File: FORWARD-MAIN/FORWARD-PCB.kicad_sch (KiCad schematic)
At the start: 50 parts, among them J1 USB_B_Micro, J3 Conn_01x13_Socket, J4 Conn_01x08_Socket, J5 Screw_Terminal_01x03, Q1 SS8050-G, Q2 SS8050-G, U2 CP2102N-Axx-xQFN28, U5 ESP32-WROOM-32D

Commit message: PCB order rev 1.0
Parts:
- removed J3: Conn_01x13_Socket, Connector_Phoenix_MSTB:PhoenixContact_MSTBA_2,5_13-G_1x13_P5.00mm_Horizontal, symbol Connector:Conn_01x13_Socket
- removed R15, R19: 3.2k, Resistor_SMD:R_0805_2012Metric, symbol Device:R_US
- removed TP4: TestPoint, Connector_PinHeader_2.54mm:PinHeader_1x01_P2.54mm_Vertical, symbol Connector:TestPoint
- added J2: Conn_01x14_Socket, Connector_PinSocket_2.54mm:PinSocket_1x14_P2.54mm_Horizontal, symbol Connector:Conn_01x14_Socket
- added J3, J6: Conn_01x02_Pin, Connector_PinSocket_2.54mm:PinSocket_1x02_P2.54mm_Vertical, symbol Connector:Conn_01x02_Pin
- Boot1, Reset1: footprint Button_Switch_SMD:SW_Tactile_SPST_NO_Straight_CK_PTS636Sx25SMTRLFS -> Button_Switch_SMD:SW_SPST_TL3305A
- D6: value LED -> Power-LED
- J5: footprint TerminalBlock_MetzConnect:TerminalBlock_MetzConnect_Type086_RT03403HBLC_1x03_P3.81mm_Horizontal -> TerminalBlock_Phoenix:TerminalBlock_Phoenix_MPT-0,5-3-2.54_1x03_P2.54mm_Horizontal
- R12: value 22.1k -> 1k
- R13: value 47.5k -> 1k
- R14: value 2k -> 10k
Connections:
- net +3.3V: now also J6.1 (Pin_1), J6.2 (Pin_2)
- net +5V: now also U2.8 (VBUS); no longer C3.1, C5.1, R14.2, U2.6 (VDD)
- net GND: now also R12.1, R13.2, J2.14 (Pin_14); no longer D6.1 (K), R13.1
- net Haptics-ENA_PWM: now also J2.5 (Pin_5)
- net Haptics-ENB_PWM: now also J2.6 (Pin_6)
- net Haptics-IN1: now also J2.1 (Pin_1)
- net Haptics-IN2: now also J2.2 (Pin_2)
- net Haptics-IN3: now also J2.3 (Pin_3)
- net Haptics-IN4: now also J2.4 (Pin_4)
- net IO0: now also U5.25 (IO0); no longer D4.2 (A)
- net LIGHT-IO4-26: now also D4.2 (A), U5.24 (IO2), J2.9 (Pin_9); no longer U5.26 (IO4)
- net P0W-IO13-16: now also J2.7 (Pin_7)
- net PHOTO-IO2-24: now also U5.26 (IO4), J2.8 (Pin_8); no longer U5.24 (IO2)
- net SCL: now also J3.2 (Pin_2)
- net SDA: now also J3.1 (Pin_1)
- net VBUS: no longer R12.1
- net Wheel_L_LPWM: now also J2.10 (Pin_10)
- net Wheel_L_RPWM: now also J2.11 (Pin_11)
- net Wheel_R_LPWM: now also J2.12 (Pin_12)
- net Wheel_R_RPWM: now also J2.13 (Pin_13)
- net at D4.1 (K): now also R12.2; no longer U5.25 (IO0)
- new net: C3.1, C5.1, R14.2, U2.6 (VDD)
- new net: D6.1 (K), R13.1
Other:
- moved on the sheet: C10, C3, C4, C5, D6, J5, R16, R17, R18, R20

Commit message: MAIN PCB rev 2.0
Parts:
- J1: footprint Connector_USB:USB_Micro-B_Molex-105133-0031 -> Connector_USB:USB_Micro-B_Wuerth_629105150521

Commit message: backups
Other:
- note added: "Harmonic Cancellation"
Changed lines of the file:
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@@
 	)
 	(rectangle
-		(start 16.51 143.51)
-		(end 58.42 190.5)
+		(start 22.86 152.4)
+		(end 49.53 181.61)
 		(stroke
 			(width 0)
@@
 		)
 	)
+	(text "Harmonic Cancellation"
+		(exclude_from_sim no)
+		(at 68.834 158.75 0)
+		(effects
+			(font
+				(size 1.27 1.27)
+			)
+			(justify left bottom)
+		)
+	)
 	(text "output only"
 		(exclude_from_sim no)
@@
 	(text "3.3V communication"
 		(exclude_from_sim no)
-		(at 27.94 27.94 0)
+		(at 50.038 23.368 0)
 		(effects
 			(font
@@
 	(text "IMU"
 		(exclude_from_sim no)
-		(at 17.78 147.32 0)
+		(at 28.194 158.496 0)
 		(effects
 			(font
@@
 		(dnp no)
 		(property "Reference" "J2"
-			(at 161.29 170.1799 0)
+			(at 161.036 175.006 0)
 			(effects
 				(font
@@
 		)
 		(property "Value" "Conn_01x14_Socket"
-			(at 161.29 172.7199 0)
+			(at 161.29 172.7199 90)
 			(effects
 				(font

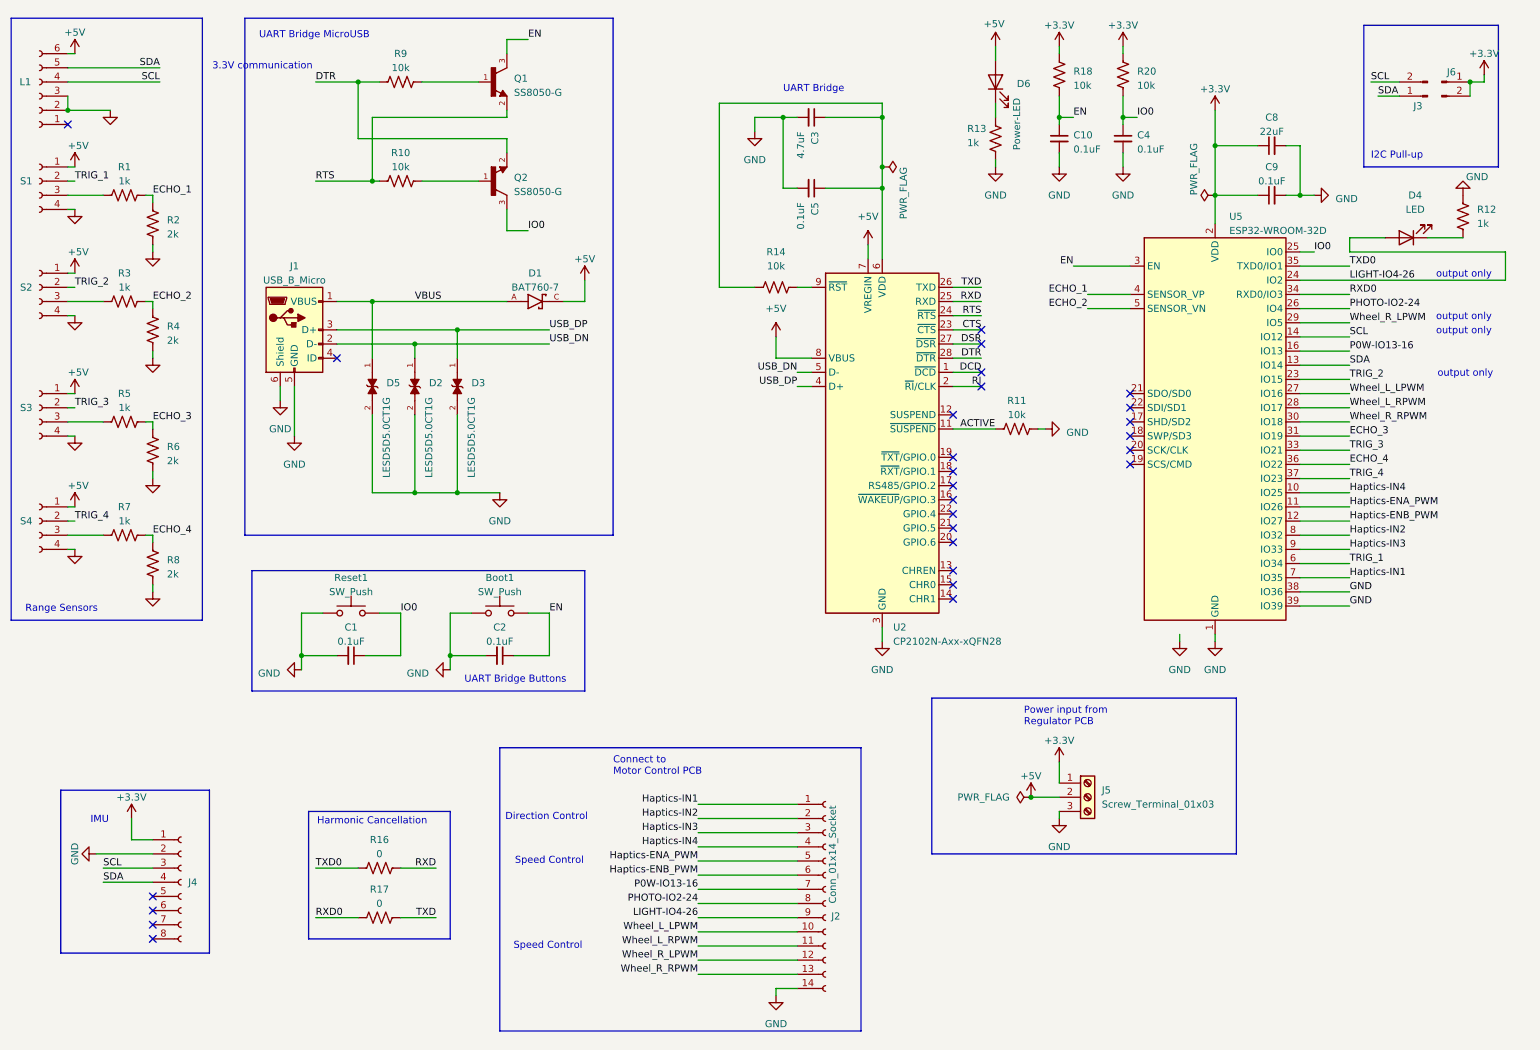
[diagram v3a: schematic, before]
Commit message: fix i2c but still an issue
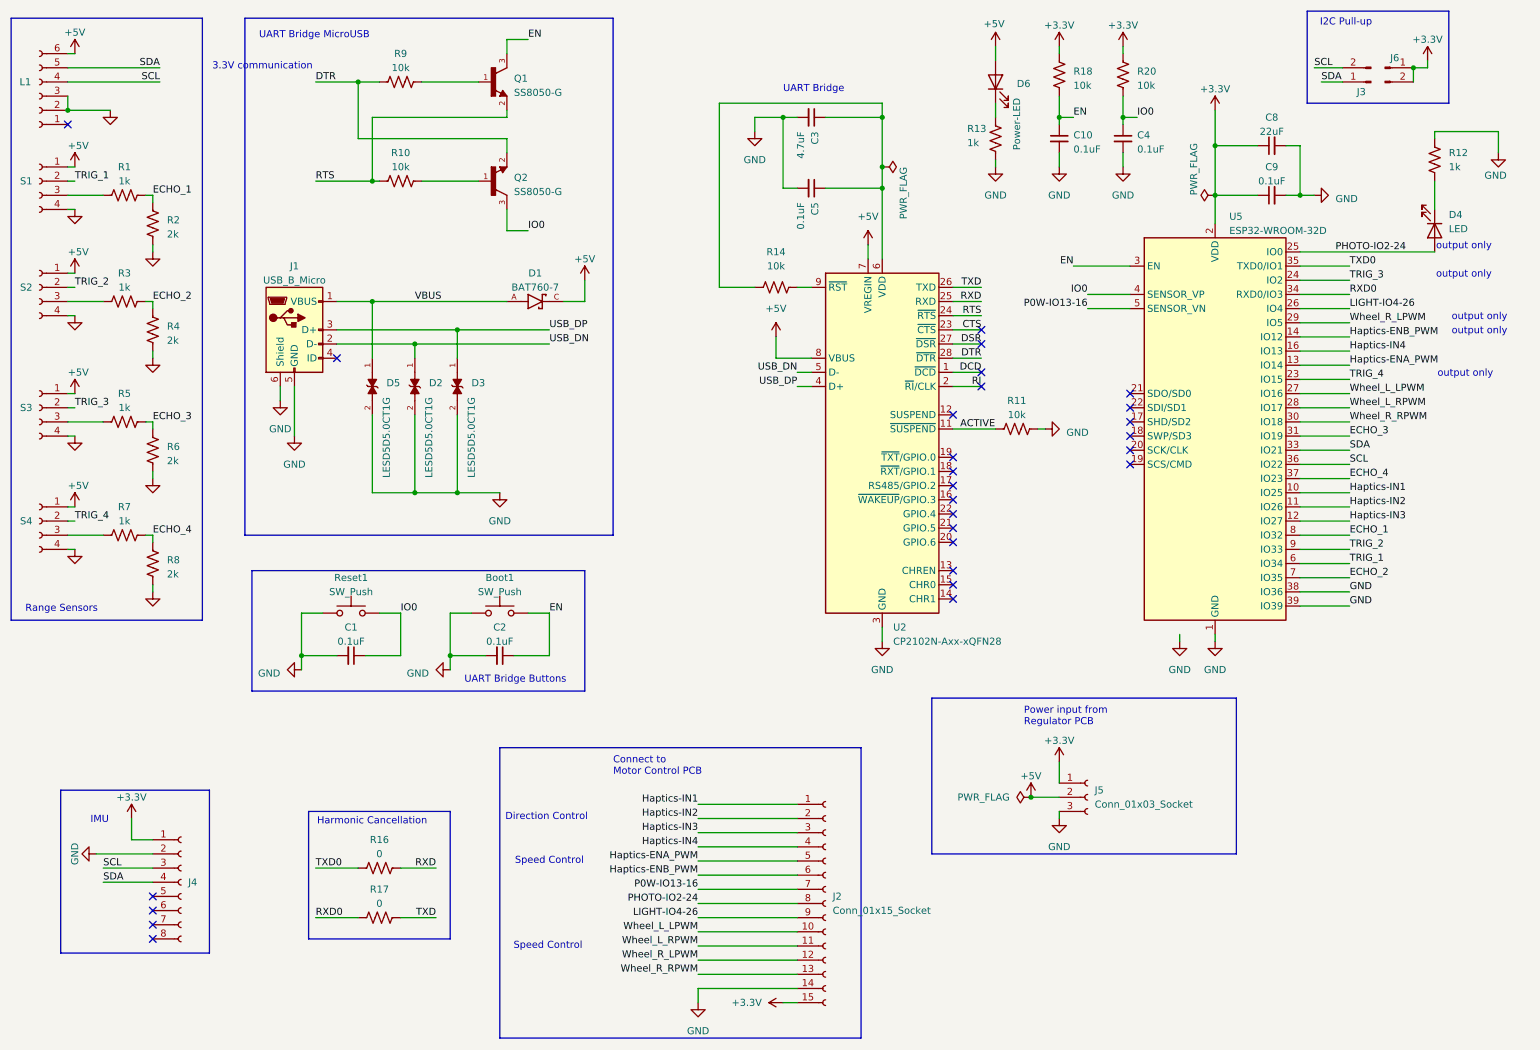
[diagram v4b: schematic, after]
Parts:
- removed J2: Conn_01x14_Socket, Connector_PinSocket_2.54mm:PinSocket_1x14_P2.54mm_Horizontal, symbol Connector:Conn_01x14_Socket
- removed J5: Screw_Terminal_01x03, TerminalBlock_Phoenix:TerminalBlock_Phoenix_MPT-0,5-3-2.54_1x03_P2.54mm_Horizontal, symbol Connector:Screw_Terminal_01x03
- added J2: Conn_01x15_Socket, Connector_PinSocket_2.54mm:PinSocket_1x15_P2.54mm_Horizontal, symbol Connector:Conn_01x15_Socket
- added J5: Conn_01x03_Socket, Connector_PinSocket_2.54mm:PinSocket_1x03_P2.54mm_Horizontal, symbol Connector:Conn_01x03_Socket
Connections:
- net +3.3V: now also J2.15 (Pin_15), J5.1 (Pin_1)
- net +5V: now also J5.2 (Pin_2)
- net ECHO_1: now also U5.8 (IO32); no longer U5.4 (SENSOR_VP)
- net ECHO_2: now also U5.7 (IO35); no longer U5.5 (SENSOR_VN)
- net ECHO_4: now also U5.37 (IO23); no longer U5.36 (IO22)
- net GND: now also J2.14 (Pin_14), J5.3 (Pin_3)
- net Haptics-ENA_PWM: now also U5.13 (IO14), J2.5 (Pin_5); no longer U5.11 (IO26)
- net Haptics-ENB_PWM: now also U5.14 (IO12), J2.6 (Pin_6); no longer U5.12 (IO27)
- net Haptics-IN1: now also U5.10 (IO25), J2.1 (Pin_1); no longer U5.7 (IO35)
- net Haptics-IN2: now also U5.11 (IO26), J2.2 (Pin_2); no longer U5.8 (IO32)
- net Haptics-IN3: now also U5.12 (IO27), J2.3 (Pin_3); no longer U5.9 (IO33)
- net Haptics-IN4: now also U5.16 (IO13), J2.4 (Pin_4); no longer U5.10 (IO25)
- net IO0: now also U5.4 (SENSOR_VP); no longer U5.25 (IO0)
- net LIGHT-IO4-26: now also U5.26 (IO4), J2.9 (Pin_9); no longer D4.2 (A), U5.24 (IO2)
- net P0W-IO13-16: now also U5.5 (SENSOR_VN), J2.7 (Pin_7); no longer U5.16 (IO13)
- net PHOTO-IO2-24: now also D4.2 (A), U5.25 (IO0), J2.8 (Pin_8); no longer U5.26 (IO4)
- net SCL: now also U5.36 (IO22); no longer U5.14 (IO12)
- net SDA: now also U5.33 (IO21); no longer U5.13 (IO14)
- net TRIG_2: now also U5.9 (IO33); no longer U5.23 (IO15)
- net TRIG_3: now also U5.24 (IO2); no longer U5.33 (IO21)
- net TRIG_4: now also U5.23 (IO15); no longer U5.37 (IO23)
- net Wheel_L_LPWM: now also J2.10 (Pin_10)
- net Wheel_L_RPWM: now also J2.11 (Pin_11)
- net Wheel_R_LPWM: now also J2.12 (Pin_12)
- net Wheel_R_RPWM: now also J2.13 (Pin_13)
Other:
- moved on the sheet: D4, J3, J6, R12

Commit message: transfer to pc
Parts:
- removed D4: LED, LED_SMD:LED_0805_2012Metric, symbol Device:LED
- removed R12: 1k, Resistor_SMD:R_0805_2012Metric, symbol Device:R_US
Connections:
- net ECHO_1: now also U5.6 (IO34); no longer U5.8 (IO32)
- net EN: now also C1.1, Reset1.2; no longer Boot1.2, C2.1
- net PHOTO-IO2-24: now also U5.4 (SENSOR_VP); no longer U5.25 (IO0)
- net TRIG_1: now also U5.8 (IO32); no longer U5.6 (IO34)
- net IO0 renamed BOOT
- net BOOT: now also Boot1.2, C2.1; no longer C1.1, Reset1.2, U5.4 (SENSOR_VP)
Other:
- moved on the sheet: Boot1, C1, C2, Reset1

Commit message: newest
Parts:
- added D4: LED, symbol Device:LED
- added R12: 1k, Resistor_SMD:R_0805_2012Metric, symbol Device:R_US
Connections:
- net BOOT: now also U5.25 (IO0)
- net ECHO_3: now also U5.33 (IO21); no longer U5.31 (IO19)
- net LIGHT-IO4-26: now also U5.23 (IO15); no longer U5.26 (IO4)
- net SCL: now also U5.29 (IO5); no longer U5.36 (IO22)
- net SDA: now also U5.30 (IO18); no longer U5.33 (IO21)
- net TRIG_3: now also U5.31 (IO19); no longer U5.24 (IO2)
- net TRIG_4: now also U5.36 (IO22); no longer U5.23 (IO15)
- net Wheel_R_LPWM: now also U5.24 (IO2); no longer U5.29 (IO5)
- net Wheel_R_RPWM: now also U5.26 (IO4); no longer U5.30 (IO18)

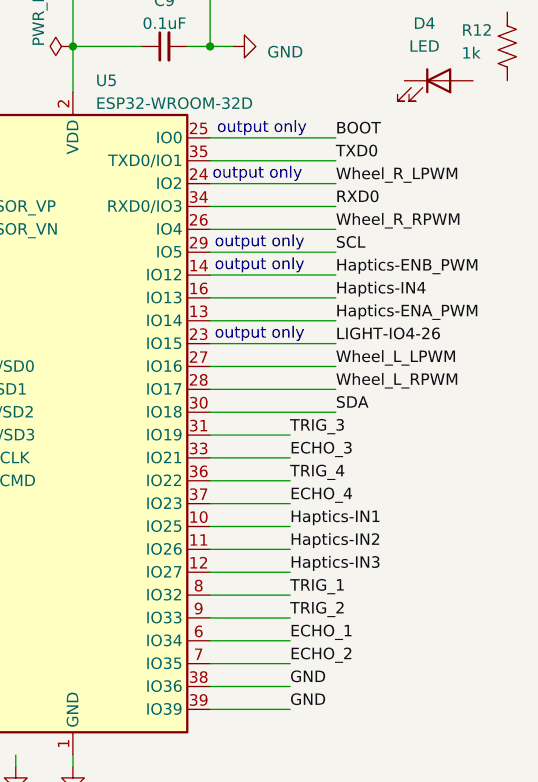
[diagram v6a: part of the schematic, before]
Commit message: finalized i2c on 3233
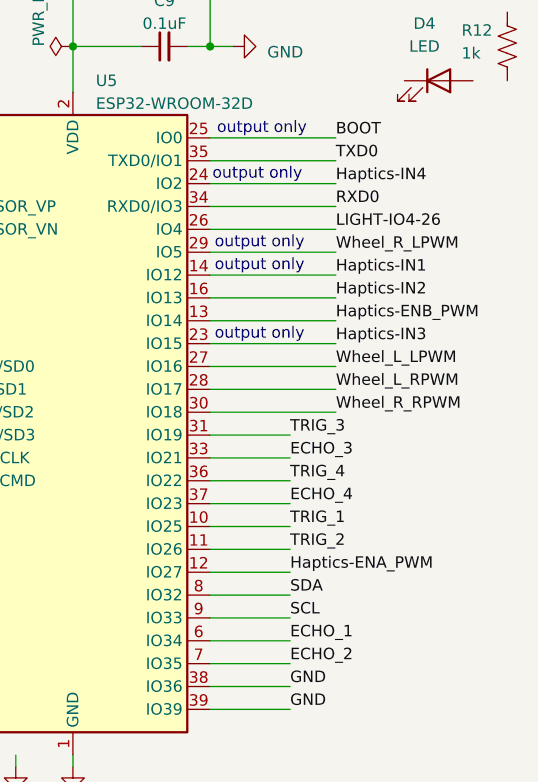
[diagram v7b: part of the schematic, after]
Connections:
- net Haptics-ENA_PWM: now also U5.12 (IO27); no longer U5.13 (IO14)
- net Haptics-ENB_PWM: now also U5.13 (IO14); no longer U5.14 (IO12)
- net Haptics-IN1: now also U5.14 (IO12); no longer U5.10 (IO25)
- net Haptics-IN2: now also U5.16 (IO13); no longer U5.11 (IO26)
- net Haptics-IN3: now also U5.23 (IO15); no longer U5.12 (IO27)
- net Haptics-IN4: now also U5.24 (IO2); no longer U5.16 (IO13)
- net LIGHT-IO4-26: now also U5.26 (IO4); no longer U5.23 (IO15)
- net SCL: now also U5.9 (IO33); no longer U5.29 (IO5)
- net SDA: now also U5.8 (IO32); no longer U5.30 (IO18)
- net TRIG_1: now also U5.10 (IO25); no longer U5.8 (IO32)
- net TRIG_2: now also U5.11 (IO26); no longer U5.9 (IO33)
- net Wheel_R_LPWM: now also U5.29 (IO5); no longer U5.24 (IO2)
- net Wheel_R_RPWM: now also U5.30 (IO18); no longer U5.26 (IO4)
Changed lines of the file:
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@@
+		)
+	)
+	(label "Haptics-ENB_PWM"
+		(at 259.08 76.2 0)
+		(fields_autoplaced yes)
+		(effects
+			(font
+				(size 1.27 1.27)
+			)
+			(justify left bottom)
 		)
 	)
@@
 		)
 	)
+	(label "Haptics-ENA_PWM"
+		(at 254 104.14 0)
+		(fields_autoplaced yes)
+		(effects
+			(font
+				(size 1.27 1.27)
+			)
+			(justify left bottom)
+		)
+	)
 	(label "SCL"
 		(at 247.65 22.86 0)
@@
 	)
 	(label "Wheel_R_LPWM"
+		(at 259.08 68.58 0)
+		(fields_autoplaced yes)
+		(effects
+			(font
+				(size 1.27 1.27)
+			)
+			(justify left bottom)
+		)
+	)
+	(label "Wheel_R_LPWM"
 		(at 137.16 182.88 180)
 		(fields_autoplaced yes)
@@
 		)
 	)
-	(label "Haptics-IN4"
-		(at 259.08 73.66 0)
-		(fields_autoplaced yes)
-		(effects
-			(font
-				(size 1.27 1.27)
-			)
-			(justify left bottom)
-		)
-	)
-	(label "Haptics-IN2"
-		(at 254 101.6 0)
-		(fields_autoplaced yes)
-		(effects
-			(font
-				(size 1.27 1.27)
-			)
-			(justify left bottom)
-		)
-	)
 	(label "USB_DP"
 		(at 154.94 80.01 180)
@@
 		)
 	)
-	(label "Haptics-ENB_PWM"
-		(at 259.08 71.12 0)
-		(fields_autoplaced yes)
-		(effects
-			(font
-				(size 1.27 1.27)
-			)
-			(justify left bottom)
-		)
-	)
 	(label "GND"
 		(at 254 116.84 0)
@@
 		)
 	)
+	(label "Haptics-IN2"
+		(at 259.08 73.66 0)
+		(fields_autoplaced yes)
+		(effects
+			(font
+				(size 1.27 1.27)
+			)
+			(justify left bottom)
+		)
+	)
 	(label "Haptics-ENB_PWM"
 		(at 137.16 167.64 180)
@@
 		)
 	)
-	(label "Wheel_R_RPWM"
-		(at 259.08 66.04 0)
+	(label "SCL"
+		(at 254 109.22 0)
+		(fields_autoplaced yes)
+		(effects
+			(font
+				(size 1.27 1.27)
+			)
+			(justify left bottom)
+		)
+	)
+	(label "TRIG_2"
+		(at 254 101.6 0)
 		(fields_autoplaced yes)
 		(effects
@@
 		)
 	)
-	(label "Wheel_R_LPWM"
-		(at 259.08 60.96 0)
-		(fields_autoplaced yes)
-		(effects
-			(font
-				(size 1.27 1.27)
-			)
-			(justify left bottom)
-		)
-	)
 	(label "DTR"
 		(at 68.58 25.4 0)
@@
 		)
 	)
-	(label "TRIG_1"
-		(at 254 106.68 0)
+	(label "Haptics-IN1"
+		(at 259.08 71.12 0)
+		(fields_autoplaced yes)
+		(effects
+			(font
+				(size 1.27 1.27)
+			)
+			(justify left bottom)
+		)
+	)
+	(label "Wheel_R_RPWM"
+		(at 259.08 86.36 0)
 		(fields_autoplaced yes)
 		(effects
@@
 		)
 	)
-	(label "LIGHT-IO4-26"
-		(at 259.08 78.74 0)
-		(fields_autoplaced yes)
-		(effects
-			(font
-				(size 1.27 1.27)
-			)
-			(justify left bottom)
-		)
-	)
 	(label "P0W-IO13-16"
 		(at 137.16 170.18 180)
@@
 		)
 	)
+	(label "Haptics-IN3"
+		(at 259.08 78.74 0)
+		(fields_autoplaced yes)
+		(effects
+			(font
+				(size 1.27 1.27)
+			)
+			(justify left bottom)
+		)
+	)
 	(label "Wheel_L_LPWM"
 		(at 259.08 81.28 0)
@@
 		)
 	)
-	(label "Haptics-ENA_PWM"
-		(at 259.08 76.2 0)
-		(fields_autoplaced yes)
-		(effects
-			(font
-				(size 1.27 1.27)
-			)
-			(justify left bottom)
-		)
-	)
 	(label "Wheel_R_RPWM"
 		(at 137.16 185.42 180)
@@
 		)
 	)
+	(label "LIGHT-IO4-26"
+		(at 259.08 66.04 0)
+		(fields_autoplaced yes)
+		(effects
+			(font
+				(size 1.27 1.27)
+			)
+			(justify left bottom)
+		)
+	)
 	(label "ECHO_1"
 		(at 254 111.76 0)
@@
 		)
 	)
-	(label "SCL"
-		(at 259.08 68.58 0)
-		(fields_autoplaced yes)
-		(effects
-			(font
-				(size 1.27 1.27)
-			)
-			(justify left bottom)
-		)
-	)
-	(label "Haptics-IN3"
-		(at 254 104.14 0)
+	(label "SDA"
+		(at 254 106.68 0)
 		(fields_autoplaced yes)
 		(effects
@@
 		)
 	)
+	(label "TRIG_1"
+		(at 254 99.06 0)
+		(fields_autoplaced yes)
+		(effects
+			(font
+				(size 1.27 1.27)
+			)
+			(justify left bottom)
+		)
+	)
 	(label "ECHO_4"
 		(at 39.37 106.68 0)
@@
 		)
 	)
-	(label "SDA"
-		(at 259.08 86.36 0)
-		(fields_autoplaced yes)
-		(effects
-			(font
-				(size 1.27 1.27)
-			)
-			(justify left bottom)
-		)
-	)
 	(label "TXD0"
 		(at 68.58 166.37 0)
@@
 		)
 	)
-	(label "TRIG_2"
-		(at 254 109.22 0)
-		(fields_autoplaced yes)
-		(effects
-			(font
-				(size 1.27 1.27)
-			)
-			(justify left bottom)
-		)
-	)
 	(label "ECHO_2"
 		(at 254 114.3 0)
@@
 		)
 	)
-	(label "Haptics-IN1"
-		(at 254 99.06 0)
-		(fields_autoplaced yes)
-		(effects
-			(font
-				(size 1.27 1.27)
-			)
-			(justify left bottom)
-		)
-	)
 	(label "SDA"
 		(at 40.64 22.86 180)
@@
 		)
 	)
+	(label "Haptics-IN4"
+		(at 259.08 60.96 0)
+		(fields_autoplaced yes)
+		(effects
+			(font
+				(size 1.27 1.27)
+			)
+			(justify left bottom)
+		)
+	)

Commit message: re-routing rev 2.0
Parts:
- removed D4: LED, symbol Device:LED
- removed J3, J6: Conn_01x02_Pin, Connector_PinSocket_2.54mm:PinSocket_1x02_P2.54mm_Vertical, symbol Connector:Conn_01x02_Pin
- removed J4: Conn_01x08_Socket, Connector_PinSocket_2.54mm:PinSocket_1x08_P2.54mm_Vertical, symbol Connector:Conn_01x08_Socket
- removed J5: Conn_01x03_Socket, Connector_PinSocket_2.54mm:PinSocket_1x03_P2.54mm_Horizontal, symbol Connector:Conn_01x03_Socket
- removed L1: Conn_01x06_Socket, Connector_PinSocket_2.54mm:PinSocket_1x06_P2.54mm_Horizontal, symbol Connector:Conn_01x06_Socket
- removed R12: 1k, Resistor_SMD:R_0805_2012Metric, symbol Device:R_US
- added H1, H2, H3, H4: MountingHole, MountingHole:MountingHole_2.2mm_M2, symbol Mechanical:MountingHole
- added J3: Screw_Terminal_01x03, TerminalBlock_Phoenix:TerminalBlock_Phoenix_PT-1,5-3-3.5-H_1x03_P3.50mm_Horizontal, symbol Connector:Screw_Terminal_01x03
- added J5: Conn_01x04_Socket, Connector_PinSocket_2.54mm:PinSocket_1x04_P2.54mm_Vertical, symbol Connector:Conn_01x04_Socket
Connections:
- net +3.3V: now also J3.1 (Pin_1), J5.1 (Pin_1)
- net +5V: now also J3.2 (Pin_2)
- net GND: now also J3.3 (Pin_3), J5.2 (Pin_2)
- net Haptics-ENA_PWM: now also J2.1 (Pin_1); no longer J2.5 (Pin_5)
- net Haptics-ENB_PWM: now also J2.2 (Pin_2); no longer J2.6 (Pin_6)
- net Haptics-IN1: now also J2.3 (Pin_3); no longer J2.1 (Pin_1)
- net Haptics-IN2: now also J2.4 (Pin_4); no longer J2.2 (Pin_2)
- net Haptics-IN3: now also J2.5 (Pin_5); no longer J2.3 (Pin_3)
- net Haptics-IN4: now also J2.6 (Pin_6); no longer J2.4 (Pin_4)
- net SCL: now also J5.3 (Pin_3)
- net SDA: now also J5.4 (Pin_4)
- no-connect marks 27 -> 22
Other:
- note removed: "I2C Pull-up"
